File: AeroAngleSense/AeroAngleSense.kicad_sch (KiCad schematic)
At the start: 18 parts, among them IC1 TPS62842DGRR, IC2 STM32F042F6P6, IC3 TMP127EDBVRQ1

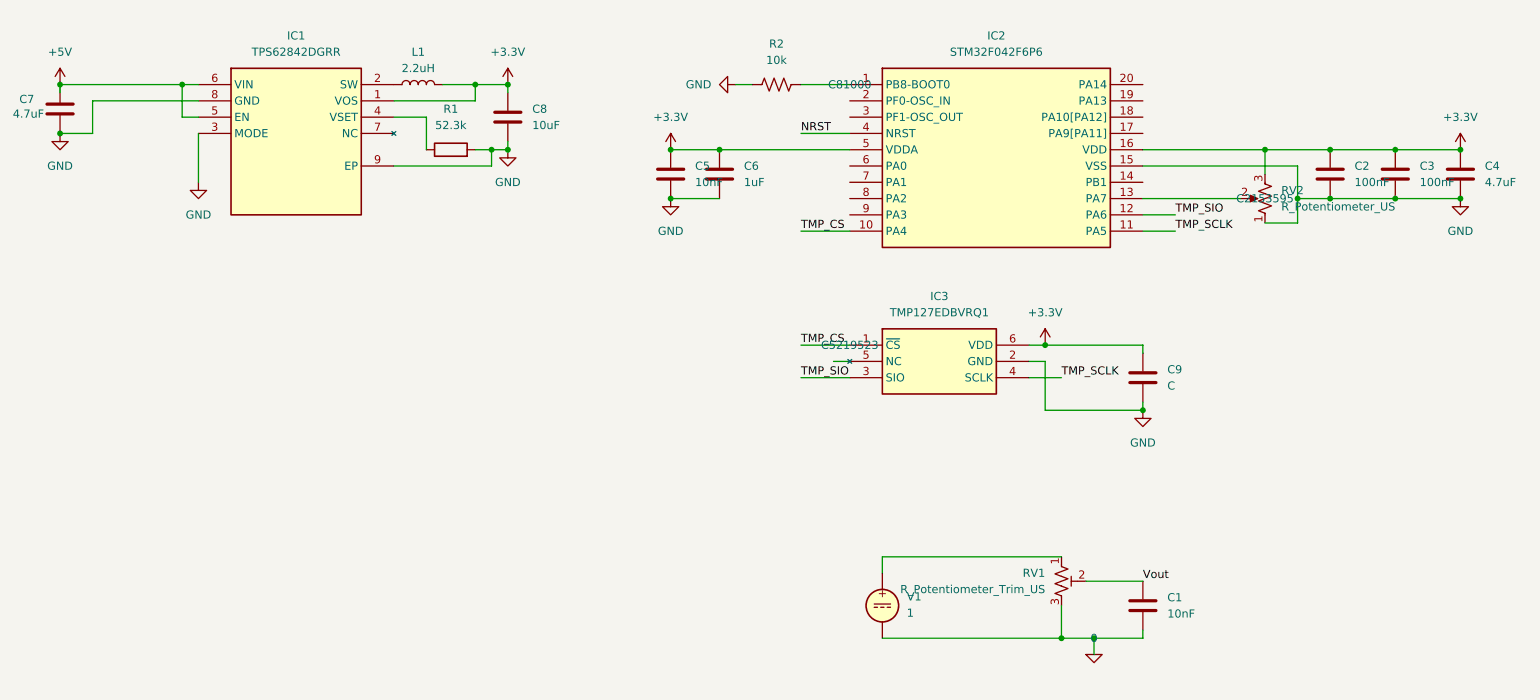
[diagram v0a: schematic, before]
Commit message: fix:temp spi 3 wire/pot_sen symbol
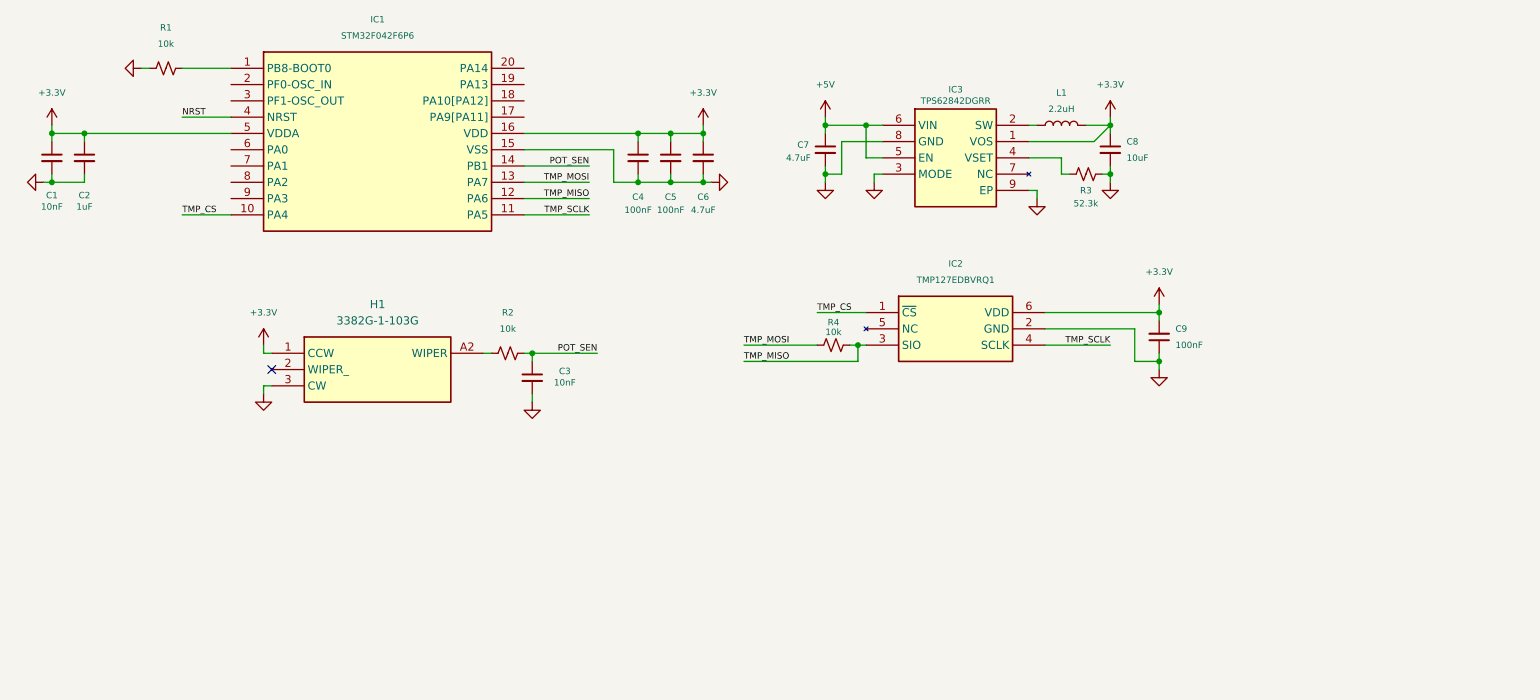
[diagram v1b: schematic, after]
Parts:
- removed C1: 10nF, symbol Device:C
- removed RV1: R_Potentiometer_Trim_US, symbol Device:R_Potentiometer_Trim_US
- removed RV2: R_Potentiometer_US, symbol Device:R_Potentiometer_US
- removed V1: 1, symbol Simulation_SPICE:VDC
- added C3: 10nF, symbol Device:C_Small
- added H1: 3382G-1-103G, 3382G1103G, symbol 3382G-1-103G:3382G-1-103G
- added R2, R4: 10k, symbol Device:R_Small_US
- C1: renamed from C5; symbol Device:C -> Device:C_Small
- C2: renamed from C6; symbol Device:C -> Device:C_Small
- C4: renamed from C2; symbol Device:C -> Device:C_Small
- C5: renamed from C3; symbol Device:C -> Device:C_Small
- C6: renamed from C4; symbol Device:C -> Device:C_Small
- C7, C8: symbol Device:C -> Device:C_Small
- C9: value C -> 100nF; symbol Device:C -> Device:C_Small
- R1: renamed from R2; symbol Device:R_US -> Device:R_Small_US
- R3: renamed from R1; symbol Device:R -> Device:R_Small_US
- renumbered IC2 to IC1, IC3 to IC2, IC1 to IC3
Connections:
- net +3.3V: now also H1.1 (CCW)
- net GND: now also C3.2, H1.3 (CW)
- net TMP_MOSI: now reaches IC1.13 (PA7)
- net TMP_MOSI: now also R4.1
- net POT_SEN: now reaches IC1.14 (PB1)
- net POT_SEN: now also C3.1, R2.2
- net TMP_SIO renamed TMP_MISO
- net TMP_MISO: now also R4.2
- new net: H1.A2 (WIPER), R2.1
- no-connect marks 0 -> 1
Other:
- moved on the sheet: C1, C2, C4, C5, C6, C7, C8, C9, IC1, IC2, IC3, L1

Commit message: LCSC값 추가
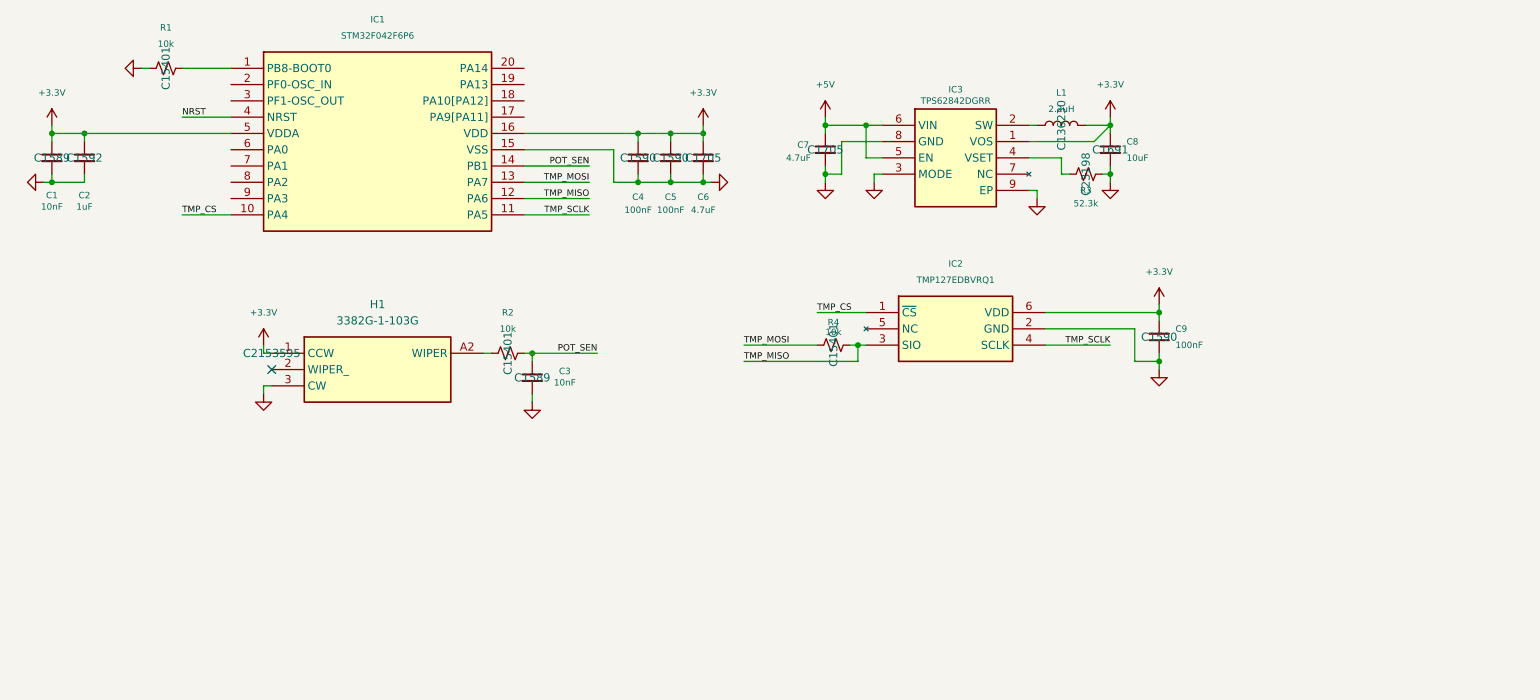
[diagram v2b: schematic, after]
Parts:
- C1, C3: LCSC (none) -> C1589
- C2: LCSC (none) -> C1592
- C4, C5, C9: LCSC (none) -> C1590
- C6, C7: LCSC (none) -> C1705
- C8: LCSC (none) -> C1691
- H1: LCSC (none) -> C2153595
- L1: LCSC (none) -> C136230
- R1, R2, R4: LCSC (none) -> C15401
- R3: LCSC (none) -> C23198

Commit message: add:DEBUG&I2C conn
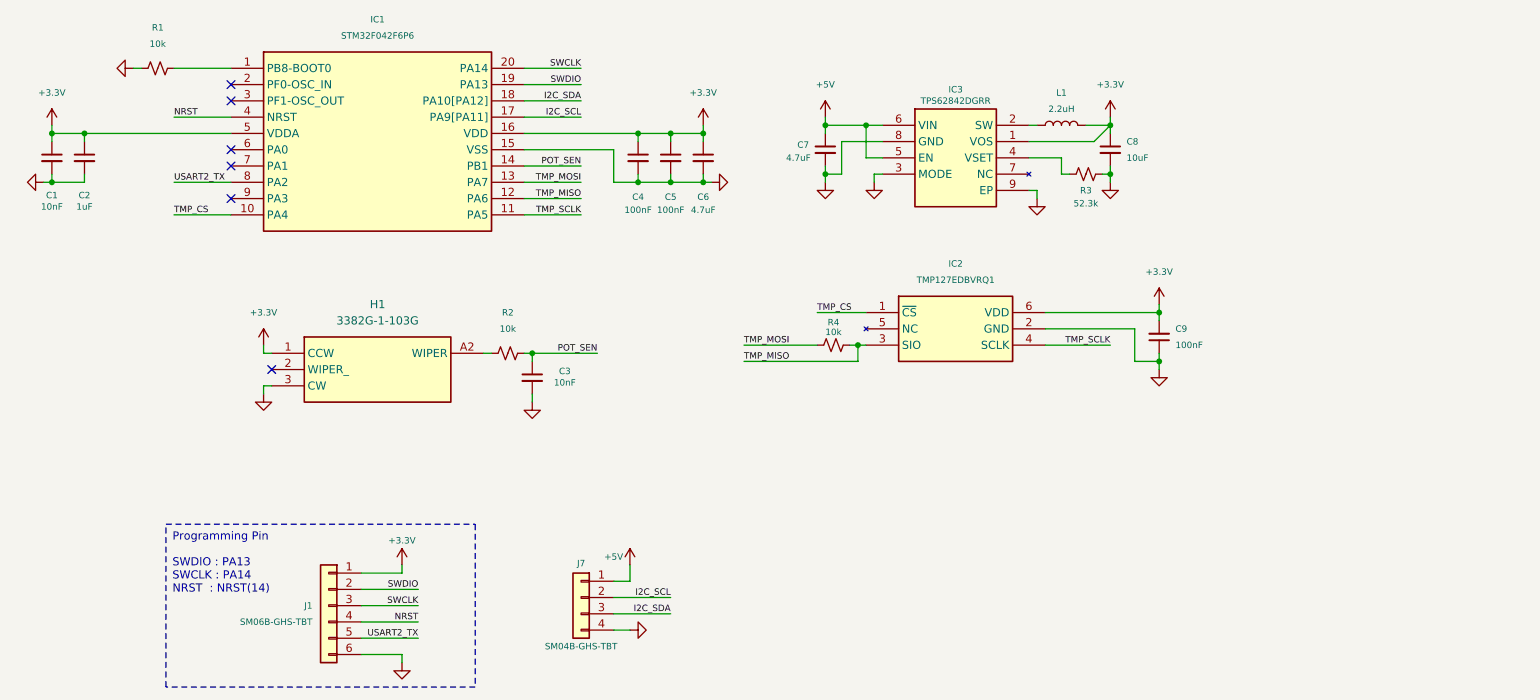
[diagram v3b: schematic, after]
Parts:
- added J1: SM06B-GHS-TBT, JST_GH:JST_GH_SM06B-GHS-TB_06x1.25mm_Angled, symbol Connector_Generic:Conn_01x06
- added J7: SM04B-GHS-TBT, JST_GH:JST_GH_SM04B-GHS-TB_04x1.25mm_Angled, symbol Connector_Generic:Conn_01x04
- H1: footprint 3382G1103G -> 3382G1103G:3382G1103G
- IC1: footprint SOP65P640X120-20N -> STM32F042F6P6:STM32F042F6P6
- IC2: footprint SOT95P280X145-6N -> TMP127EDBVRQ1:SOT95P280X145-6N
- IC3: footprint SOP65P490X110-9N -> TPS62842DGRR:TPS62842DGRR
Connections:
- net +3.3V: now also J1.1 (Pin_1)
- net +5V: now also J7.1 (Pin_1)
- net GND: now also J1.6 (Pin_6), J7.4 (Pin_4)
- net NRST: now also J1.4 (Pin_4)
- net I2C_SCL: now reaches IC1.17 (PA9[PA11])
- net I2C_SCL: now also J7.2 (Pin_2)
- net I2C_SDA: now reaches IC1.18 (PA10[PA12])
- net I2C_SDA: now also J7.3 (Pin_3)
- net SWDIO: now reaches IC1.19 (PA13)
- net SWDIO: now also J1.2 (Pin_2)
- net SWCLK: now reaches IC1.20 (PA14)
- net SWCLK: now also J1.3 (Pin_3)
- net USART2_TX: now reaches IC1.8 (PA2)
- net USART2_TX: now also J1.5 (Pin_5)
- no-connect marks 1 -> 6
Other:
- note added: "Programming Pin"
- note added: "SWDIO : PA13 SWCLK : PA14 NRST : NRST(14)"
- moved on the sheet: R1

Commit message: 소자 배치
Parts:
- C1, C2, C3, C4, C5, C6, C7, C8, C9: footprint (none) -> Capacitor_SMD:C_0603_1608Metric
- J1: footprint JST_GH:JST_GH_SM06B-GHS-TB_06x1.25mm_Angled -> JST_GH_SM:JST_GH_SM06B-GHS-TB_06x1.25mm_Angled
- J7: footprint JST_GH:JST_GH_SM04B-GHS-TB_04x1.25mm_Angled -> JST_GH_SM:JST_GH_SM04B-GHS-TB_04x1.25mm_Angled
- L1: footprint (none) -> VLS201610ET-2R2M:VLS201610ET-2R2M
- R1, R2, R3, R4: footprint (none) -> Resistor_SMD:R_0603_1608Metric
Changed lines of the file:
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@@
 			)
 		)
-		(property "Footprint" ""
+		(property "Footprint" "Resistor_SMD:R_0603_1608Metric"
 			(at 170.18 93.98 0)
 			(effects
@@
 			)
 		)
-		(property "Footprint" ""
+		(property "Footprint" "Capacitor_SMD:C_0603_1608Metric"
 			(at 168.91 63.5 0)
 			(effects
@@
 			)
 		)
-		(property "Footprint" ""
+		(property "Footprint" "Capacitor_SMD:C_0603_1608Metric"
 			(at 48.26 64.77 0)
 			(effects
@@
 			)
 		)
-		(property "Footprint" ""
+		(property "Footprint" "Resistor_SMD:R_0603_1608Metric"
 			(at 209.55 67.31 0)
 			(effects
@@
 			)
 		)
-		(property "Footprint" ""
+		(property "Footprint" "Capacitor_SMD:C_0603_1608Metric"
 			(at 144.78 64.77 0)
 			(effects
@@
 			)
 		)
-		(property "Footprint" ""
+		(property "Footprint" "Capacitor_SMD:C_0603_1608Metric"
 			(at 149.86 64.77 0)
 			(effects
@@
 			)
 		)
-		(property "Footprint" ""
+		(property "Footprint" "Capacitor_SMD:C_0603_1608Metric"
 			(at 123.19 99.06 0)
 			(effects
@@
 			)
 		)
-		(property "Footprint" ""
+		(property "Footprint" "VLS201610ET-2R2M:VLS201610ET-2R2M"
 			(at 205.74 59.69 0)
 			(effects
@@
 			)
 		)
-		(property "Footprint" "JST_GH:JST_GH_SM04B-GHS-TB_04x1.25mm_Angled"
+		(property "Footprint" "JST_GH_SM:JST_GH_SM04B-GHS-TB_04x1.25mm_Angled"
 			(at 130.81 133.35 0)
 			(effects
@@
 			)
 		)
-		(property "Footprint" ""
+		(property "Footprint" "Capacitor_SMD:C_0603_1608Metric"
 			(at 53.34 64.77 0)
 			(effects
@@
 			)
 		)
-		(property "Footprint" ""
+		(property "Footprint" "Resistor_SMD:R_0603_1608Metric"
 			(at 119.38 95.25 0)
 			(effects
@@
 			)
 		)
-		(property "Footprint" ""
+		(property "Footprint" "Resistor_SMD:R_0603_1608Metric"
 			(at 64.77 50.8 0)
 			(effects
@@
 			)
 		)
-		(property "Footprint" ""
+		(property "Footprint" "Capacitor_SMD:C_0603_1608Metric"
 			(at 213.36 63.5 0)
 			(effects
@@
 			)
 		)
-		(property "Footprint" "JST_GH:JST_GH_SM06B-GHS-TB_06x1.25mm_Angled"
+		(property "Footprint" "JST_GH_SM:JST_GH_SM06B-GHS-TB_06x1.25mm_Angled"
 			(at 91.44 134.62 0)
 			(effects
@@
 			)
 		)
-		(property "Footprint" ""
+		(property "Footprint" "Capacitor_SMD:C_0603_1608Metric"
 			(at 220.98 92.71 0)
 			(effects
@@
 			)
 		)
-		(property "Footprint" ""
+		(property "Footprint" "Capacitor_SMD:C_0603_1608Metric"
 			(at 139.7 64.77 0)
 			(effects
